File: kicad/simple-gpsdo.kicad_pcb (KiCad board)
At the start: 2 copper layers, 119.5 x 74.5 mm, 95 parts, among them J1 PPS_OUT, J2 PWR, J3 ISP, J6 USB_B_Micro, J7 NEO-6M, J8 10MHz_OUT, Q1 PJA3407, SW1 RST, U1 XRP6272ITC5TR-F, U2 ATmega32U4-AU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

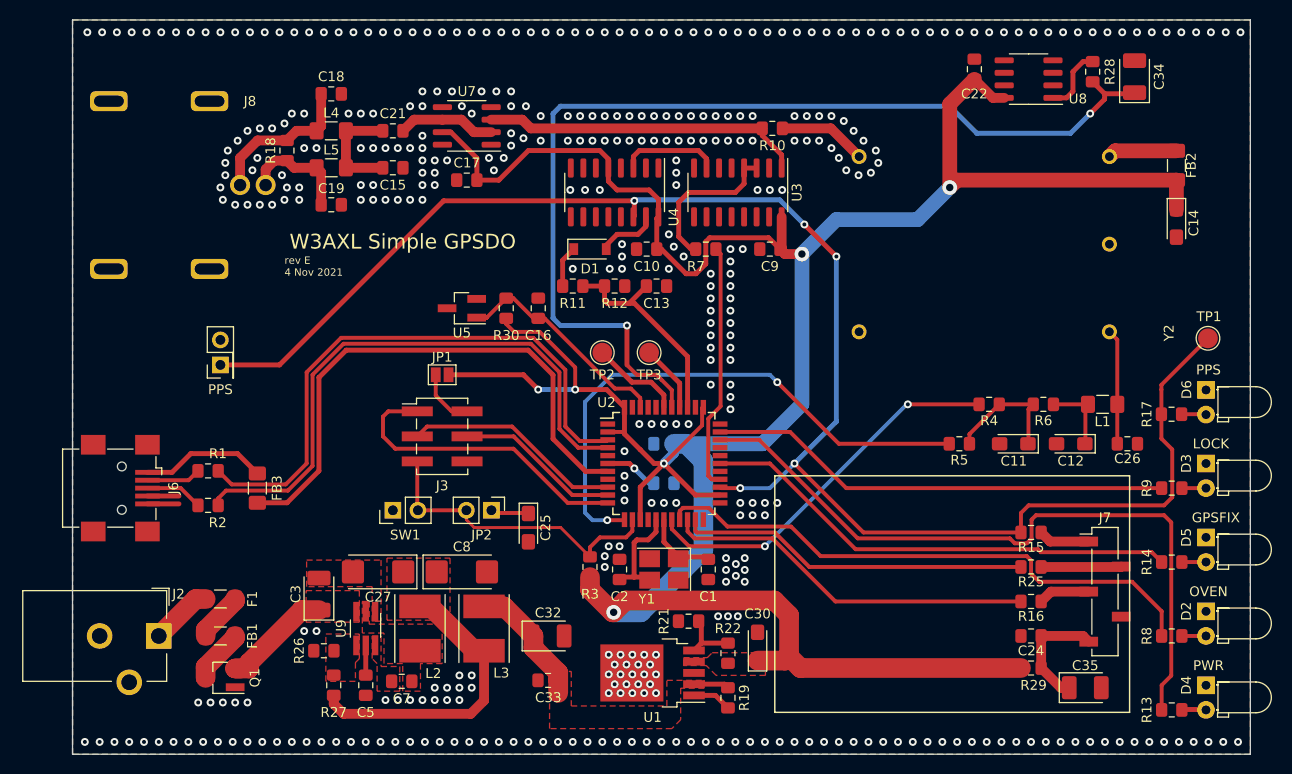
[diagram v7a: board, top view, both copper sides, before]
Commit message: lengthened pcb by 0.5mm
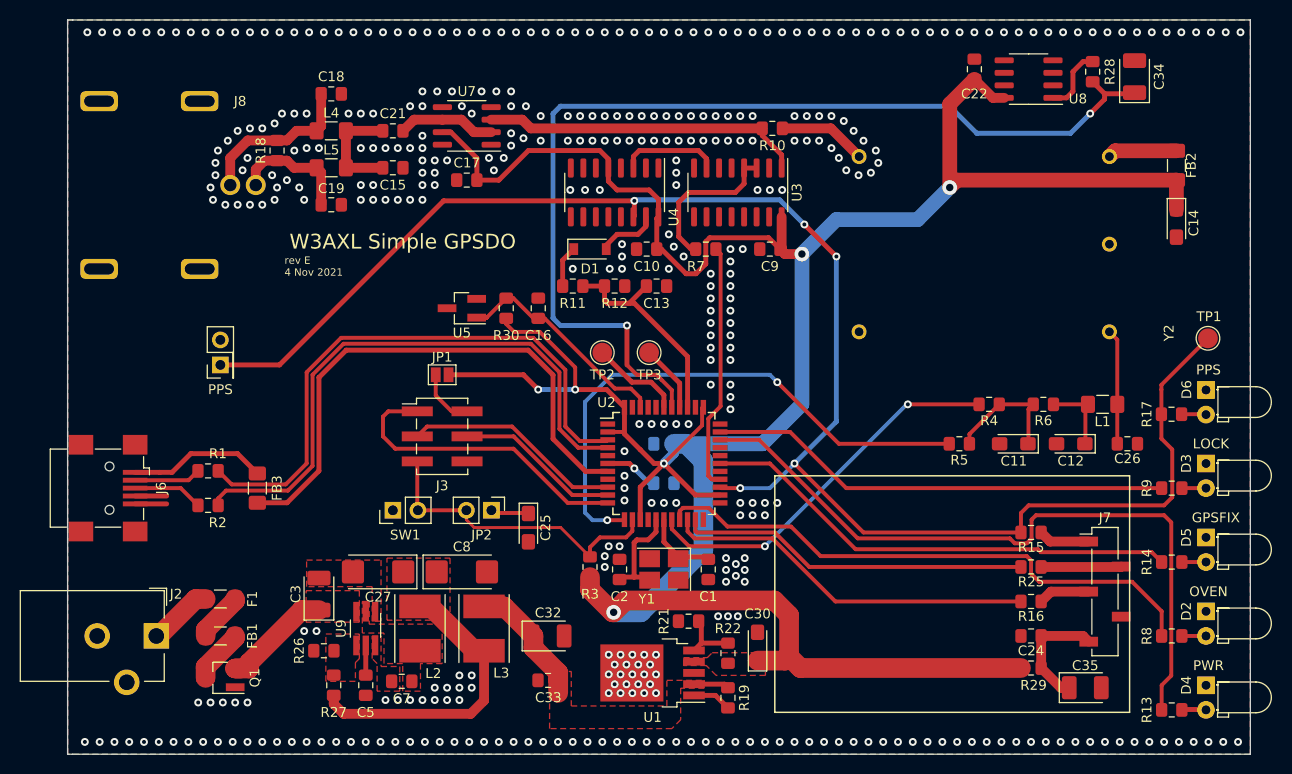
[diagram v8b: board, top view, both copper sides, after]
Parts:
- moved J6 1.25 mm to (78.8, 122.5)
- moved J8 1.00 mm to (91.0, 91.8)
- moved R18 1.00 mm to (95.8, 88.2)
- moved J2 0.25 mm to (83.5, 137.5)
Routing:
- net Net-(FB3-Pad1): track 12.8 -> 14.0 mm
- net Net-(C19-Pad1): track 11.4 -> 12.4 mm
- net Net-(C18-Pad2): track 15.6 -> 16.6 mm
- net GND: vias 395 -> 398
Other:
- board size 119.5 x 74.5 mm -> 120 x 74.5 mm
